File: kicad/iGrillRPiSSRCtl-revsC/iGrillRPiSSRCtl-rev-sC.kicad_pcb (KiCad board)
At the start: 2 copper layers, 65 x 56 mm, 27 parts, among them J1 Screw_Terminal_01x02, P1 Conn_02x20_Odd_Even, Q1 Q_NPN_ECB, Q2 Q_PNP_EBC, Q3 Q_PNP_EBC, SW1 Off On

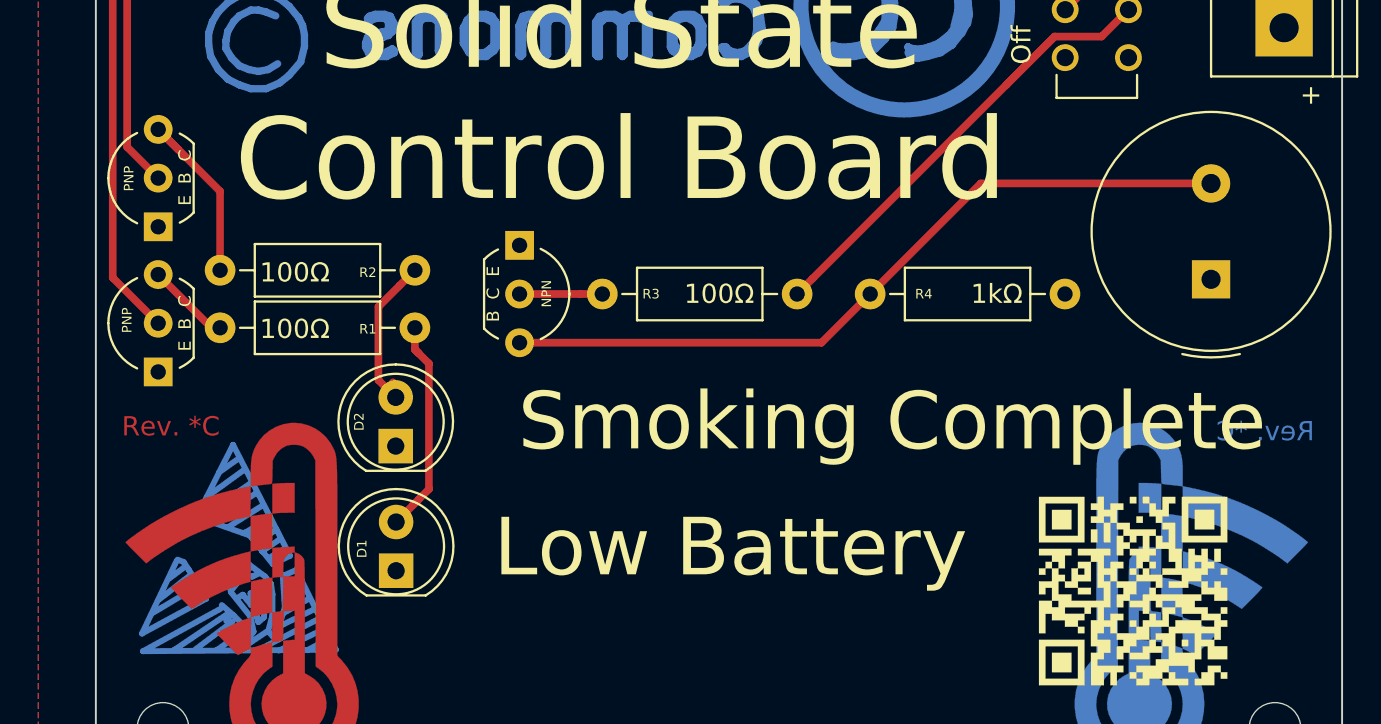
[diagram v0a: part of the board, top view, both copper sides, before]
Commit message: Moving to smd devices
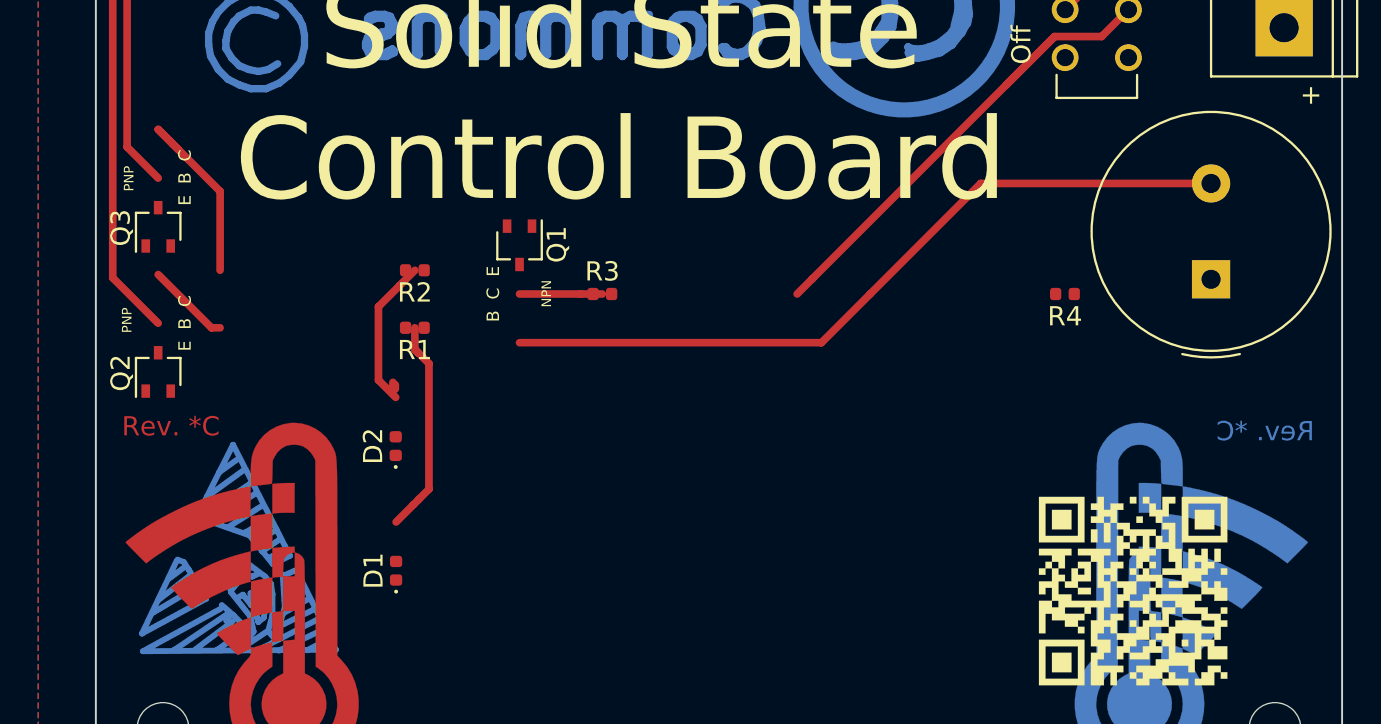
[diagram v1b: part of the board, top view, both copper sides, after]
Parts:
- D1: footprint LED_THT:LED_D5.0mm -> LED_SMD:LED_0402_1005Metric
- D2: footprint LED_THT:LED_D5.0mm_Clear -> LED_SMD:LED_0402_1005Metric
- Q1, Q2, Q3: footprint Package_TO_SOT_THT:TO-92_Inline_Wide -> Package_TO_SOT_SMD:SOT-323_SC-70
- R1, R2, R3, R4: footprint Resistor_THT:R_Axial_DIN0207_L6.3mm_D2.5mm_P10.16mm_Horizontal -> Resistor_SMD:R_0402_1005Metric
